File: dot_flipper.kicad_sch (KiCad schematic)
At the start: 1 part, among them U1 7_flip_dots

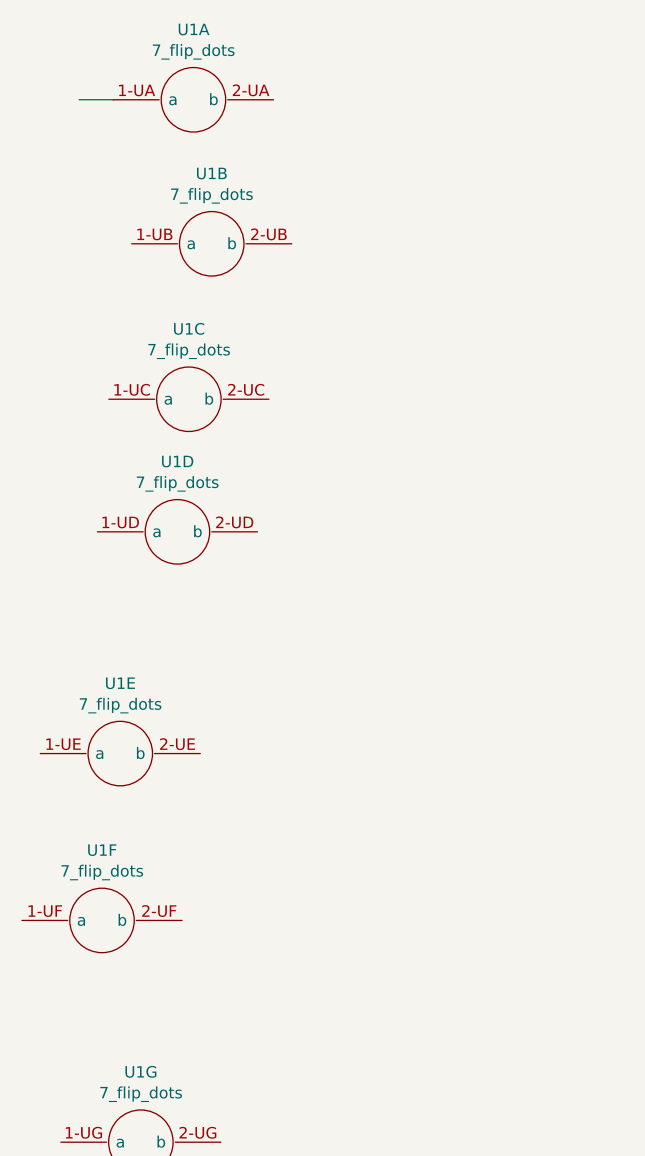
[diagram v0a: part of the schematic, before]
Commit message: Add DRV8837C
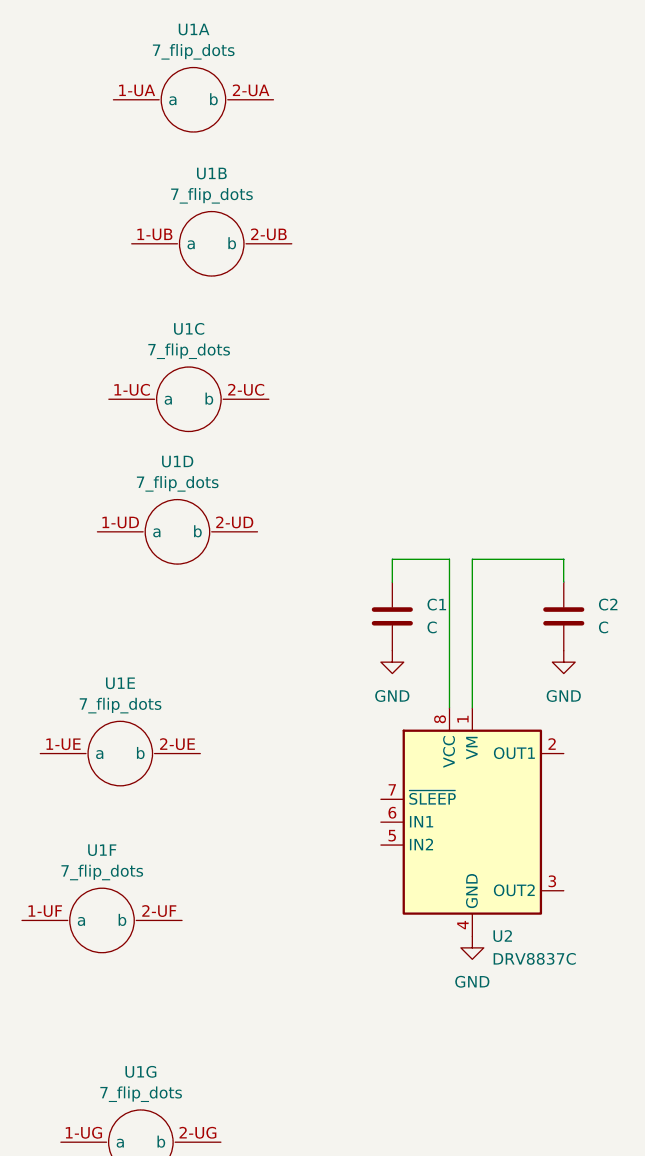
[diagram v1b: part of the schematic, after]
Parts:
- added C1, C2: C, Capacitor_SMD:C_0201_0603Metric_Pad0.64x0.40mm_HandSolder, symbol Device:C
- added U2: DRV8837C, Package_SON:WSON-8-1EP_2x2mm_P0.5mm_EP0.9x1.6mm, symbol Driver_Motor:DRV8837C
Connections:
- new net: C2.1, U2.1 (VM)
- new net: C1.1, U2.8 (VCC)
- new net GND: C1.2, C2.2, U2.4 (GND), U2.9 (GND)

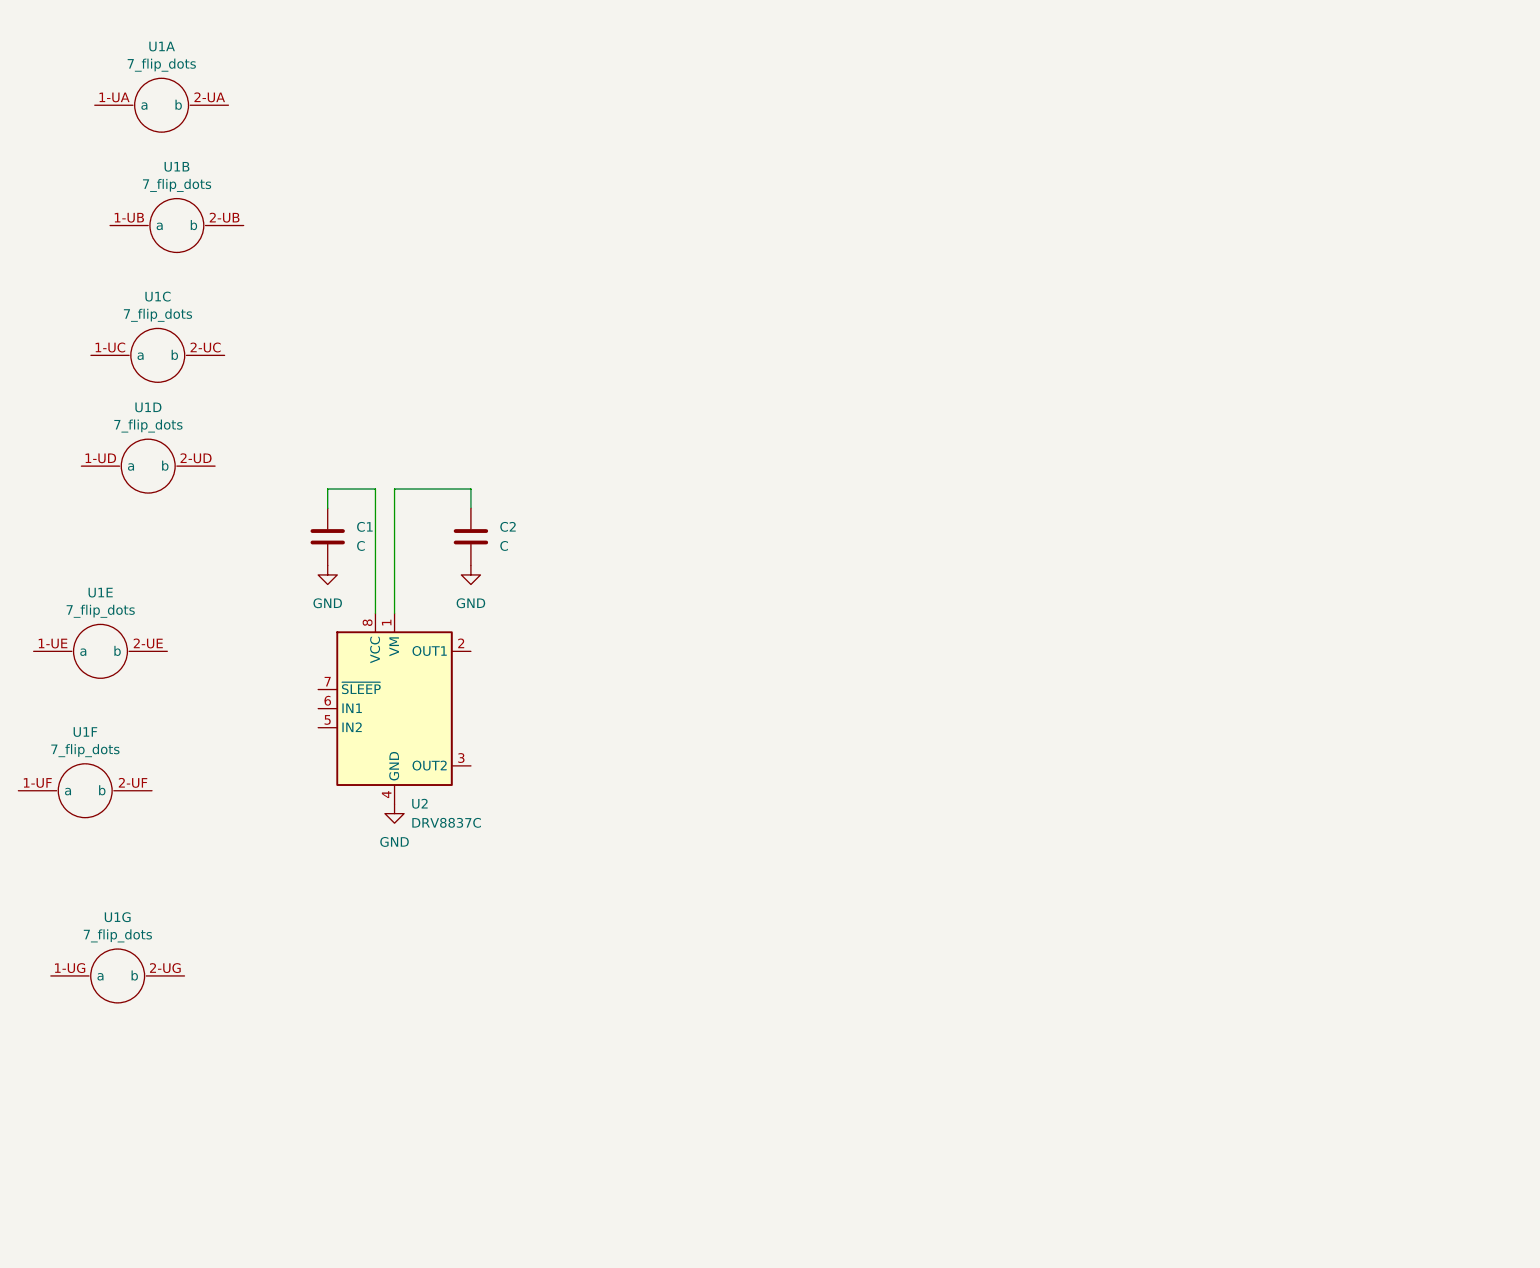
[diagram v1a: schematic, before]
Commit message: Updated with 2 H-bridges
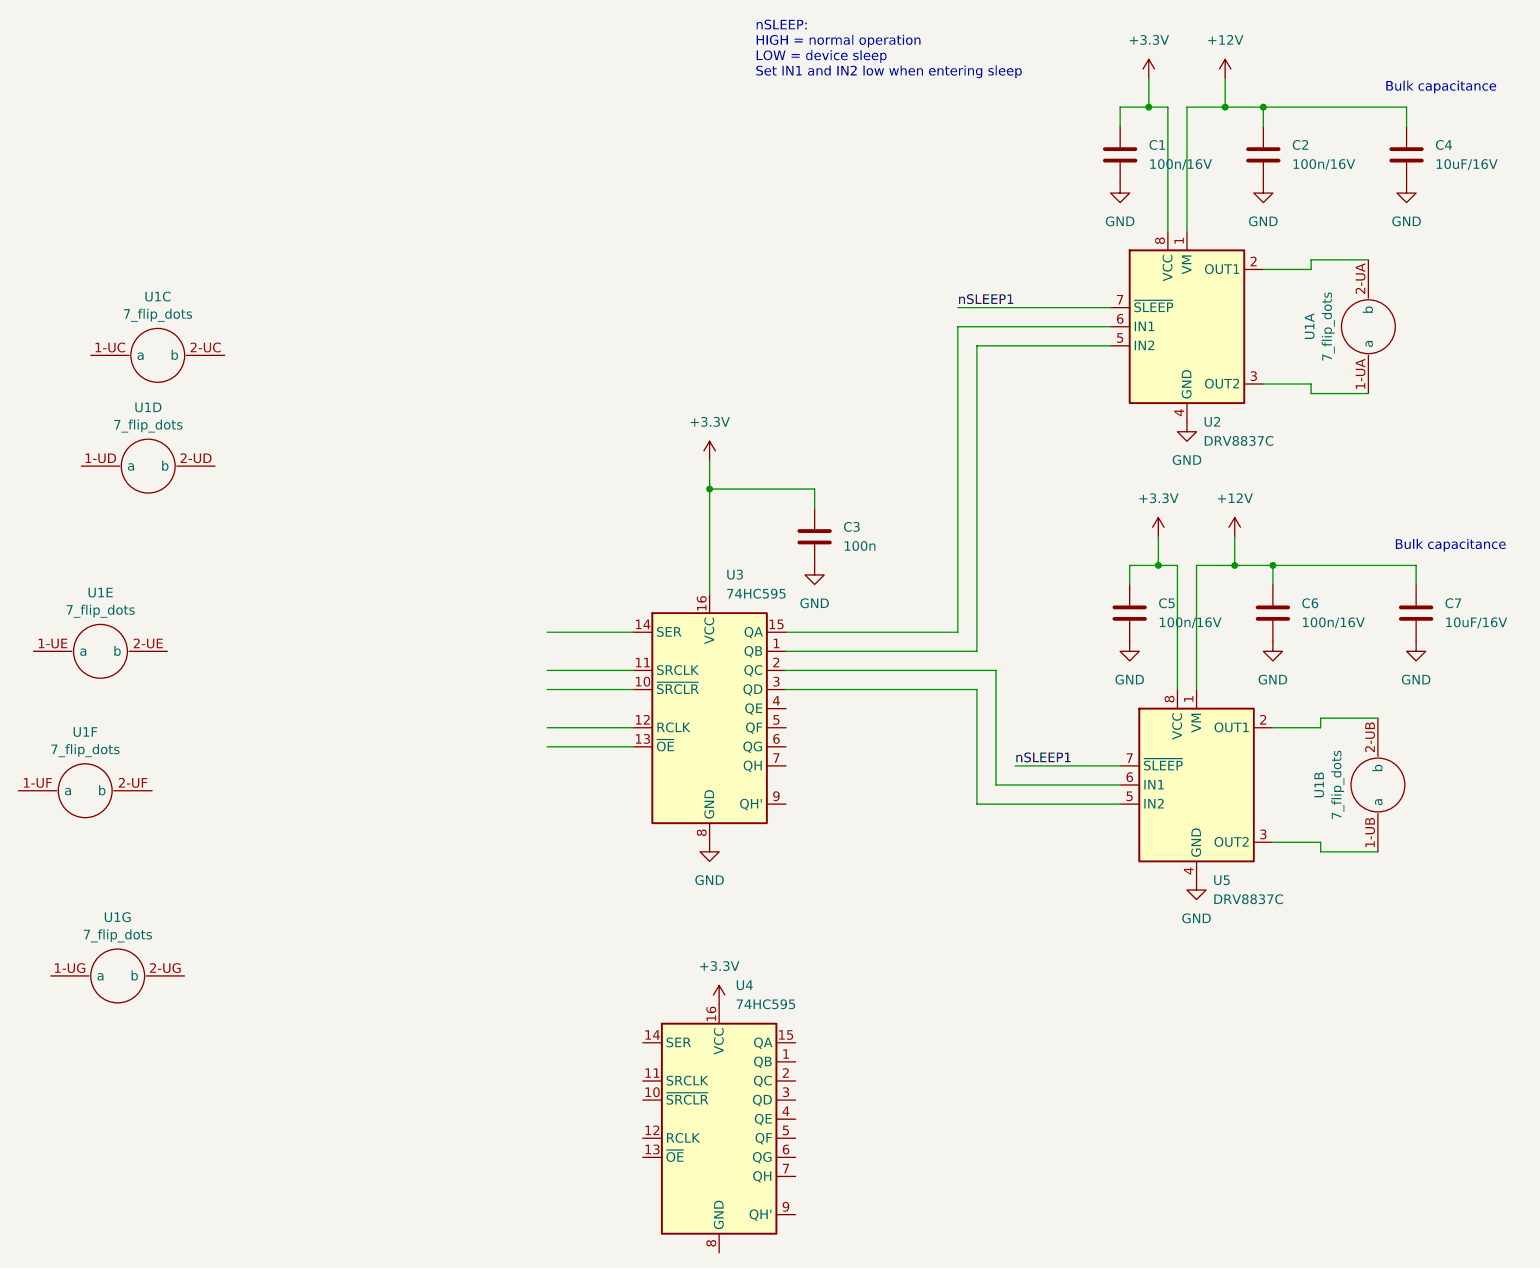
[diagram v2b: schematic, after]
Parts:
- added C3: 100n, Capacitor_SMD:C_0201_0603Metric_Pad0.64x0.40mm_HandSolder, symbol Device:C
- added C4, C7: 10uF/16V, Capacitor_SMD:C_0201_0603Metric_Pad0.64x0.40mm_HandSolder, symbol Device:C
- added C5, C6: 100n/16V, Capacitor_SMD:C_0201_0603Metric_Pad0.64x0.40mm_HandSolder, symbol Device:C
- added U3, U4: 74HC595, symbol 74xx:74HC595
- added U5: DRV8837C, Package_SON:WSON-8-1EP_2x2mm_P0.5mm_EP0.9x1.6mm, symbol Driver_Motor:DRV8837C
- C1, C2: value C -> 100n/16V
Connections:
- net GND: now also C3.2, C4.2, C5.2, C6.2, C7.2, U3.8 (GND), U5.4 (GND), U5.9 (GND)
- net at U1.1-UA (a): now also U2.3 (OUT2)
- net at U1.2-UA (b): now also U2.2 (OUT1)
- net at U1.1-UB (a): now also U5.3 (OUT2)
- net at U1.2-UB (b): now also U5.2 (OUT1)
- net +12V: now reaches C2.1, U2.1 (VM)
- net +12V: now also C4.1, C6.1, C7.1, U5.1 (VM)
- net +3.3V: now reaches C1.1, U2.8 (VCC)
- net +3.3V: now also C3.1, C5.1, U3.16 (VCC), U4.16 (VCC), U5.8 (VCC)
- net at U2.5 (IN2): now also U3.1 (QB)
- net at U2.6 (IN1): now also U3.15 (QA)
- net nSLEEP1: now reaches U2.7 (~{SLEEP})
- net nSLEEP1: now also U5.7 (~{SLEEP})
- new net: U3.3 (QD), U5.5 (IN2)
- new net: U3.2 (QC), U5.6 (IN1)
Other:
- note added: "Bulk capacitance"
- note added: "nSLEEP: HIGH = normal operation LOW = device sleep Set IN1 and IN2 low when entering sleep"
- moved on the sheet: C1, C2, U1A, U1B, U2

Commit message: Single module schematic
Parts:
- removed U4: 74HC595, symbol 74xx:74HC595
- added C10, C11, C15, C16, C17, C19, C20, C21, C8, C9: 100n/16V, Capacitor_SMD:C_0201_0603Metric_Pad0.64x0.40mm_HandSolder, symbol Device:C
- added C12, C13, C23, C24, C25: 10uF/16V, Capacitor_SMD:C_0201_0603Metric_Pad0.64x0.40mm_HandSolder, symbol Device:C
- added C14: 100n, Capacitor_SMD:C_0201_0603Metric_Pad0.64x0.40mm_HandSolder, symbol Device:C
- added J1, J2: Conn_01x06_Socket, Connector_JST:JST_XH_S6B-XH-A-1_1x06_P2.50mm_Horizontal, symbol Connector:Conn_01x06_Socket
- added J3, J4: Conn_01x06_Socket, Connector_PinSocket_2.54mm:PinSocket_1x06_P2.54mm_Vertical, symbol Connector:Conn_01x06_Socket
- added TP1: SEROUT1, TestPoint:TestPoint_Pad_D1.5mm, symbol Connector:TestPoint
- added TP2: SLEEP, TestPoint:TestPoint_Pad_D1.5mm, symbol Connector:TestPoint
- added TP3: LATCH, TestPoint:TestPoint_Pad_D1.5mm, symbol Connector:TestPoint
- added TP4: SRCLK, TestPoint:TestPoint_Pad_D1.5mm, symbol Connector:TestPoint
- added TP5: SERIN, TestPoint:TestPoint_Pad_D1.5mm, symbol Connector:TestPoint
- added TP6: VCC, TestPoint:TestPoint_Pad_D1.5mm, symbol Connector:TestPoint
- added TP7: GND, TestPoint:TestPoint_Pad_D1.5mm, symbol Connector:TestPoint
- added U10, U4, U6, U8, U9: DRV8837C, Package_SON:WSON-8-1EP_2x2mm_P0.5mm_EP0.9x1.6mm, symbol Driver_Motor:DRV8837C
- added U11, U12: CDSOT236-T05C, Package_TO_SOT_SMD:SOT-23-6, symbol Power_Protection:CDSOT236-0504C
- added U7: 74HC595, Package_SO:TSSOP-16_4.4x5mm_P0.65mm, symbol 74xx:74HC595
- U3: footprint (none) -> Package_SO:TSSOP-16_4.4x5mm_P0.65mm
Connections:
- net +3.3V is gone; now on net VCC: C1.1, C3.1, C5.1, U2.8 (VCC), U3.16 (VCC), U5.8 (VCC)
- net nSLEEP1 is gone; now on net SLEEP: U2.7 (~{SLEEP}), U5.7 (~{SLEEP})
- net GND: now also C10.2, C11.2, C12.2, C13.2, C14.2, C15.2, C16.2, C17.2, C19.2, C20.2, C21.2, C23.2, C24.2, C25.2, C8.2, C9.2, J1.6 (Pin_6), J2.6 (Pin_6), J3.1 (Pin_1), J4.1 (Pin_1), TP7.1, U10.4 (GND), U10.9 (GND), U11.2 (VN), U12.2 (VN), U4.4 (GND), U4.9 (GND), U6.4 (GND), U6.9 (GND), U7.8 (GND), U8.4 (GND), U8.9 (GND), U9.4 (GND), U9.9 (GND)
- net at U1.1-UC (a): now also U4.3 (OUT2)
- net at U1.2-UC (b): now also U4.2 (OUT1)
- net at U1.1-UD (a): now also U6.3 (OUT2)
- net at U1.2-UD (b): now also U6.2 (OUT1)
- net at U1.1-UE (a): now also U8.3 (OUT2)
- net at U1.2-UE (b): now also U8.2 (OUT1)
- net at U1.1-UF (a): now also U10.3 (OUT2)
- net at U1.2-UF (b): now also U10.2 (OUT1)
- net at U1.1-UG (a): now also U9.3 (OUT2)
- net at U1.2-UG (b): now also U9.2 (OUT1)
- net VCC: now reaches U3.10 (~{SRCLR})
- net VCC: now also C14.1, C15.1, C16.1, C17.1, C8.1, C9.1, J1.1 (Pin_1), J2.1 (Pin_1), J3.6 (Pin_6), J4.6 (Pin_6), TP6.1, U10.8 (VCC), U11.5 (VP), U12.5 (VP), U4.8 (VCC), U6.8 (VCC), U7.10 (~{SRCLR}), U7.16 (VCC), U8.8 (VCC), U9.8 (VCC)
- net SRCLK: now reaches U3.11 (SRCLK)
- net SRCLK: now also J1.3 (Pin_3), J2.3 (Pin_3), J3.4 (Pin_4), J4.4 (Pin_4), TP4.1, U11.3 (IO2), U12.3 (IO2), U7.11 (SRCLK)
- net LATCH: now reaches U3.12 (RCLK)
- net LATCH: now also J1.4 (Pin_4), J2.4 (Pin_4), J3.3 (Pin_3), J4.3 (Pin_3), TP3.1, U11.4 (IO3), U12.4 (IO3), U7.12 (RCLK)
- net SLEEP: now reaches U3.13 (~{OE})
- net SLEEP: now also J1.5 (Pin_5), J2.5 (Pin_5), J3.2 (Pin_2), J4.2 (Pin_2), TP2.1, U10.7 (~{SLEEP}), U11.6 (IO4), U12.6 (IO4), U4.7 (~{SLEEP}), U6.7 (~{SLEEP}), U7.13 (~{OE}), U8.7 (~{SLEEP}), U9.7 (~{SLEEP})
- net SERIN: now reaches U3.14 (SER)
- net SERIN: now also J1.2 (Pin_2), J3.5 (Pin_5), TP5.1, U11.1 (IO1)
- net at U3.4 (QE): now also U4.6 (IN1)
- net at U3.5 (QF): now also U4.5 (IN2)
- net at U3.6 (QG): now also U6.6 (IN1)
- net at U3.7 (QH): now also U6.5 (IN2)
- net SEROUT1: now reaches U3.9 (QH')
- net SEROUT1: now also TP1.1, U7.14 (SER)
- net +12V renamed VM
- net VM: now also C10.1, C11.1, C12.1, C13.1, C19.1, C20.1, C21.1, C23.1, C24.1, C25.1, U10.1 (VM), U4.1 (VM), U6.1 (VM), U8.1 (VM), U9.1 (VM)
- new net: U7.1 (QB), U8.5 (IN2)
- new net: U7.15 (QA), U8.6 (IN1)
- new net: U10.6 (IN1), U7.2 (QC)
- new net: U10.5 (IN2), U7.3 (QD)
- new net: U7.4 (QE), U9.6 (IN1)
- new net: U7.5 (QF), U9.5 (IN2)
- new net SEROUT2: J2.2 (Pin_2), J4.5 (Pin_5), U12.1 (IO1), U7.9 (QH')
- no-connect marks 0 -> 2
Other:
- note added: "Input Header"
- note added: "Output Header"
- note added: "Pixel 1"
- note added: "Pixel 2"
- note added: "Pixel 3"
- note added: "Pixel 4"
- note added: "Pixel 5"
- note added: "Pixel 6"
- note added: "Pixel 7"
- note added: "Shift Register 1"
- note added: "Shift Register 2"
- moved on the sheet: C1, C2, C3, C4, C5, C6, C7, U1A, U1B, U1C, U1D, U1E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

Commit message: Rough component placement
Slightly tweaked flipdot footprint to match my measurements and datasheet better
Created board outline, interfaces.
Rough component placement.
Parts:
- added TP51: SEROUT2, TestPoint:TestPoint_Pad_D1.5mm, symbol Connector:TestPoint
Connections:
- net SEROUT2: now also TP51.1
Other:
- note added: "Module 1"
- moved on the sheet: C1, C10, C11, C12, C13, C14, C15, C16, C17, C19, C2, C20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

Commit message: Cost optimisation
Removed one shift register by adding 7 signal inverters (now only need 7 shift register outputs instead of 14 to control 7 H-bridges)
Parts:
- removed C14: 100n, Capacitor_SMD:C_0201_0603Metric_Pad0.64x0.40mm_HandSolder, symbol Device:C
- removed U7: 74HC595, Package_SO:TSSOP-16_4.4x5mm_P0.65mm, symbol 74xx:74HC595
- added U13, U14, U15, U16, U17, U18, U19: 74LVC1G04, symbol 74xGxx:74LVC1G04
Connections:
- net GND: now also U13.3 (GND), U14.3 (GND), U15.3 (GND), U16.3 (GND), U17.3 (GND), U18.3 (GND), U19.3 (GND)
- net VCC: now also U13.5 (VCC), U14.5 (VCC), U15.5 (VCC), U16.5 (VCC), U17.5 (VCC), U18.5 (VCC), U19.5 (VCC)
- net at U3.7 (QH): no longer U6.5 (IN2)
- net at U6.6 (IN1): now also U16.4; no longer U3.6 (QG)
- net OUT5: now reaches U8.5 (IN2)
- net OUT5: now also U3.4 (QE), U17.2
- net at U8.6 (IN1): now also U17.4
- net at U10.6 (IN1): now also U18.4
- net OUT6: now reaches U10.5 (IN2)
- net OUT6: now also U3.5 (QF), U18.2
- net at U9.6 (IN1): now also U19.4
- net OUT7: now reaches U9.5 (IN2)
- net OUT7: now also U3.6 (QG), U19.2
- net OUT1: now reaches U2.5 (IN2)
- net OUT1: now also U3.15 (QA), U13.2; no longer U3.1 (QB)
- net at U2.6 (IN1): now also U13.4; no longer U3.15 (QA)
- net at U5.6 (IN1): now also U14.4; no longer U3.2 (QC)
- net OUT2: now reaches U5.5 (IN2)
- net OUT2: now also U3.1 (QB), U14.2; no longer U3.3 (QD)
- net at U4.6 (IN1): now also U15.4; no longer U3.4 (QE)
- net OUT3: now reaches U4.5 (IN2)
- net OUT3: now also U3.2 (QC), U15.2; no longer U3.5 (QF)
- new net OUT4: U16.2, U3.3 (QD), U6.5 (IN2)
- no-connect marks 2 -> 1
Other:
- note removed: "Shift Register 2"
- moved on the sheet: C1, C10, C11, C12, C13, C15, C16, C17, C19, C2, C20, C21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

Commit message: LCSC codes added
Also broken out VM pin to input/output headers
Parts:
- removed J1: Conn_01x06_Socket, Connector_JST:JST_XH_S6B-XH-A-1_1x06_P2.50mm_Horizontal, symbol Connector:Conn_01x06_Socket
- removed J3: Conn_01x06_Socket, Connector_PinSocket_2.54mm:PinSocket_1x06_P2.54mm_Vertical, symbol Connector:Conn_01x06_Socket
- removed U14, U16, U18, U19: 74LVC1G04, symbol 74xGxx:74LVC1G04
- added J1: INPUT, symbol Connector:Conn_01x07_Pin
- added J2: OUTPUT, symbol Connector:Conn_01x07_Socket
- added JP1: SolderJumper_2_Open, Jumper:SolderJumper-2_P1.3mm_Open_RoundedPad1.0x1.5mm, symbol Jumper:SolderJumper_2_Open
- added TP8: GND, TestPoint:TestPoint_Pad_D1.5mm, symbol Connector:TestPoint
- added U10, U13, U5, U7: SN74LVC1G04DCKR, Package_TO_SOT_SMD:SOT-353_SC-70-5, symbol 74xGxx:74LVC1G04
- U1: renamed from U13; value 74LVC1G04 -> SN74LVC1G04DCKR; footprint (none) -> Package_TO_SOT_SMD:SOT-353_SC-70-5; Digikey (none) -> 296-11600-1-ND; LCSC (none) -> C8207
- U11: renamed from U6; value DRV8837C -> DRV8837CDSGR; Digikey (none) -> 296-47205-1-ND; LCSC (none) -> C191000
- U12: Digikey (none) -> CDSOT236-T05CCT-ND; LCSC (none) -> C1973568
- U14: renamed from U8; value DRV8837C -> DRV8837CDSGR; Digikey (none) -> 296-47205-1-ND; LCSC (none) -> C191000
- U15, U17: value 74LVC1G04 -> SN74LVC1G04DCKR; footprint (none) -> Package_TO_SOT_SMD:SOT-353_SC-70-5; Digikey (none) -> 296-11600-1-ND; LCSC (none) -> C8207
- U16: renamed from U10; value DRV8837C -> DRV8837CDSGR; Digikey (none) -> 296-47205-1-ND; LCSC (none) -> C191000
- U18: renamed from U9; value DRV8837C -> DRV8837CDSGR; Digikey (none) -> 296-47205-1-ND; LCSC (none) -> C191000
- U2: value DRV8837C -> DRV8837CDSGR; Digikey (none) -> 296-47205-1-ND; LCSC (none) -> C191000
- U4: renamed from U3; value 74HC595 -> SN74HC595PWR; Digikey (none) -> 296-23258-1-ND; LCSC (none) -> C273642
- U6: renamed from U5; value DRV8837C -> DRV8837CDSGR; Digikey (none) -> 296-47205-1-ND; LCSC (none) -> C191000
- U8: renamed from U4; value DRV8837C -> DRV8837CDSGR; Digikey (none) -> 296-47205-1-ND; LCSC (none) -> C191000
- U9: renamed from U11; Digikey (none) -> CDSOT236-T05CCT-ND; LCSC (none) -> C1973568
- renumbered C12 to C10, C9 to C11, C11 to C12, C15 to C14, C19 to C15, C23 to C16, C21 to C18, C25 to C19, C16 to C20, C20 to C21, C24 to C22, C4 to C3, C3 to C4, C10 to C9, J2 to J3, TP4 to TP2, TP2 to TP4, TP51 to TP9, U1 to U3
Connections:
- net GND: now also J1.7 (Pin_7), J2.7 (Pin_7), U10.3 (GND), U13.3 (GND), U5.3 (GND), U7.3 (GND)
- net LATCH: now also J1.5 (Pin_5), J2.5 (Pin_5)
- net OUT2: now also U5.2
- net OUT3: now also U7.2; no longer U15.2
- net OUT4: now also U10.2
- net OUT5: now also U13.2; no longer U17.2
- net OUT6: now also U15.2
- net OUT7: now also U17.2
- net SERIN: now also J1.3 (Pin_3), J2.3 (Pin_3)
- net SLEEP: now also J1.6 (Pin_6), J2.6 (Pin_6)
- net SRCLK: now also J1.4 (Pin_4), J2.4 (Pin_4)
- net VCC: now also J1.2 (Pin_2), J2.2 (Pin_2), JP1.2 (B), U10.5 (VCC), U13.5 (VCC), U5.5 (VCC), U7.5 (VCC)
- net VM: now also J1.1 (Pin_1), J2.1 (Pin_1), JP1.1 (A), TP8.1
- net at U11.6 (IN1): now also U10.4
- net at U17.4: now also U18.6 (IN1); no longer U14.6 (IN1)
- net at U16.6 (IN1): now also U15.4
- net at U8.6 (IN1): now also U7.4; no longer U15.4
- net at U6.6 (IN1): now also U5.4
- new net: U13.4, U14.6 (IN1)
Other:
- moved on the sheet: C4, TP1, U4
